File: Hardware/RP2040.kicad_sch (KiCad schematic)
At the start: 22 parts, among them U1 W25Q128JVS, U2 RP2040, Y1 ABM8-272-T3

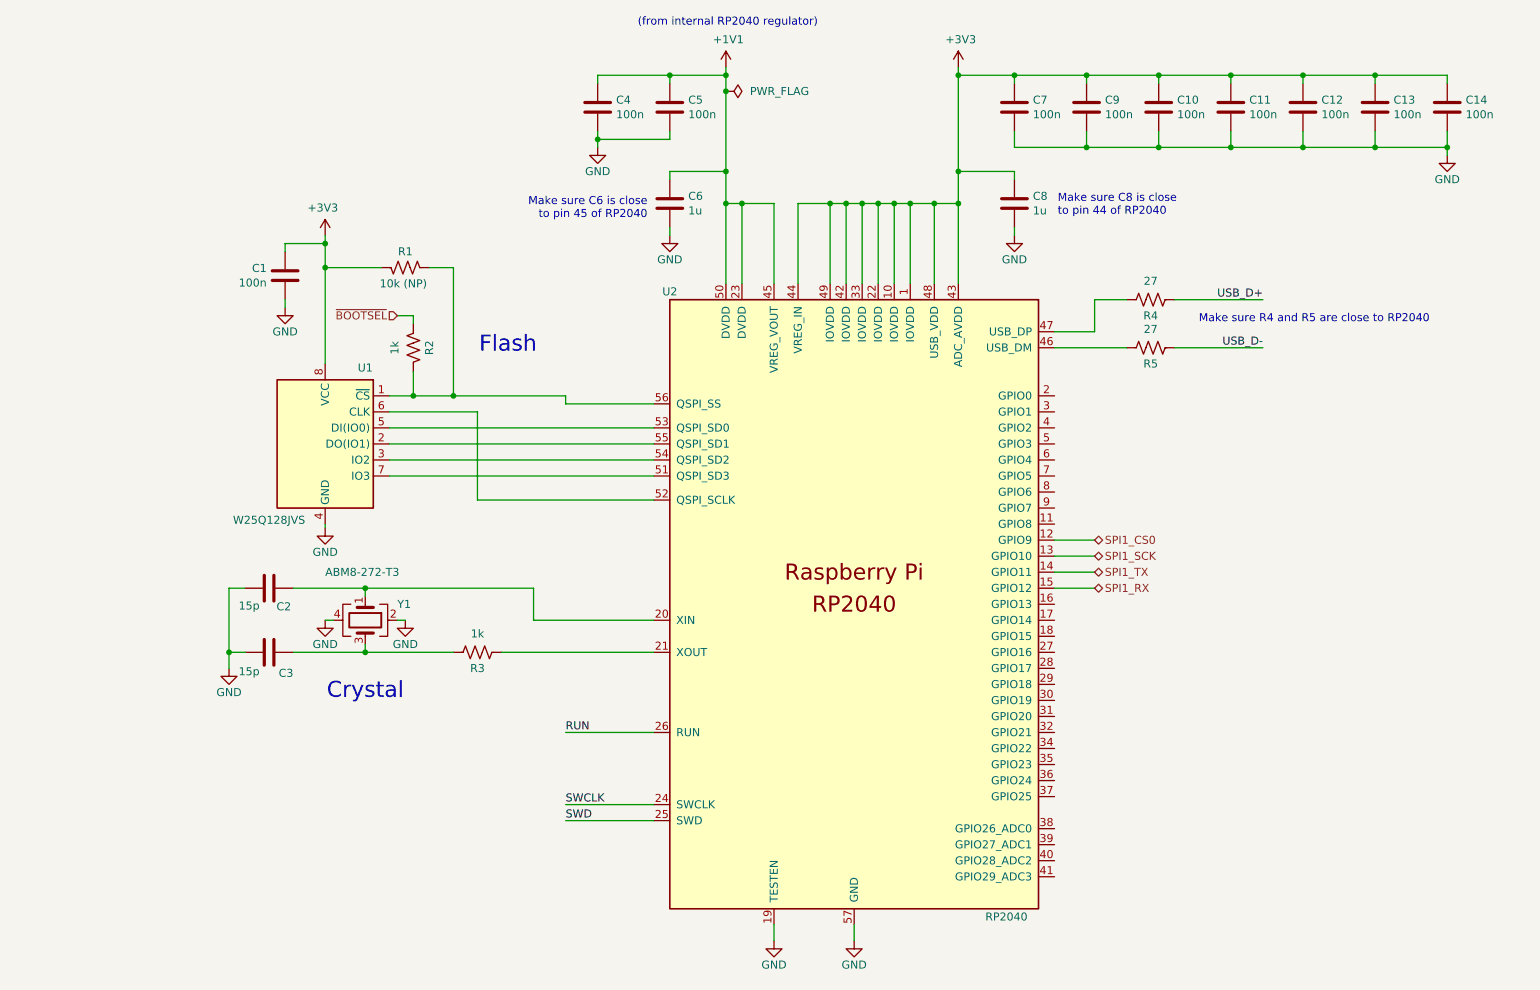
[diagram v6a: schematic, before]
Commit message: Add STM32 Reset Switch & RP2040 I2C pins
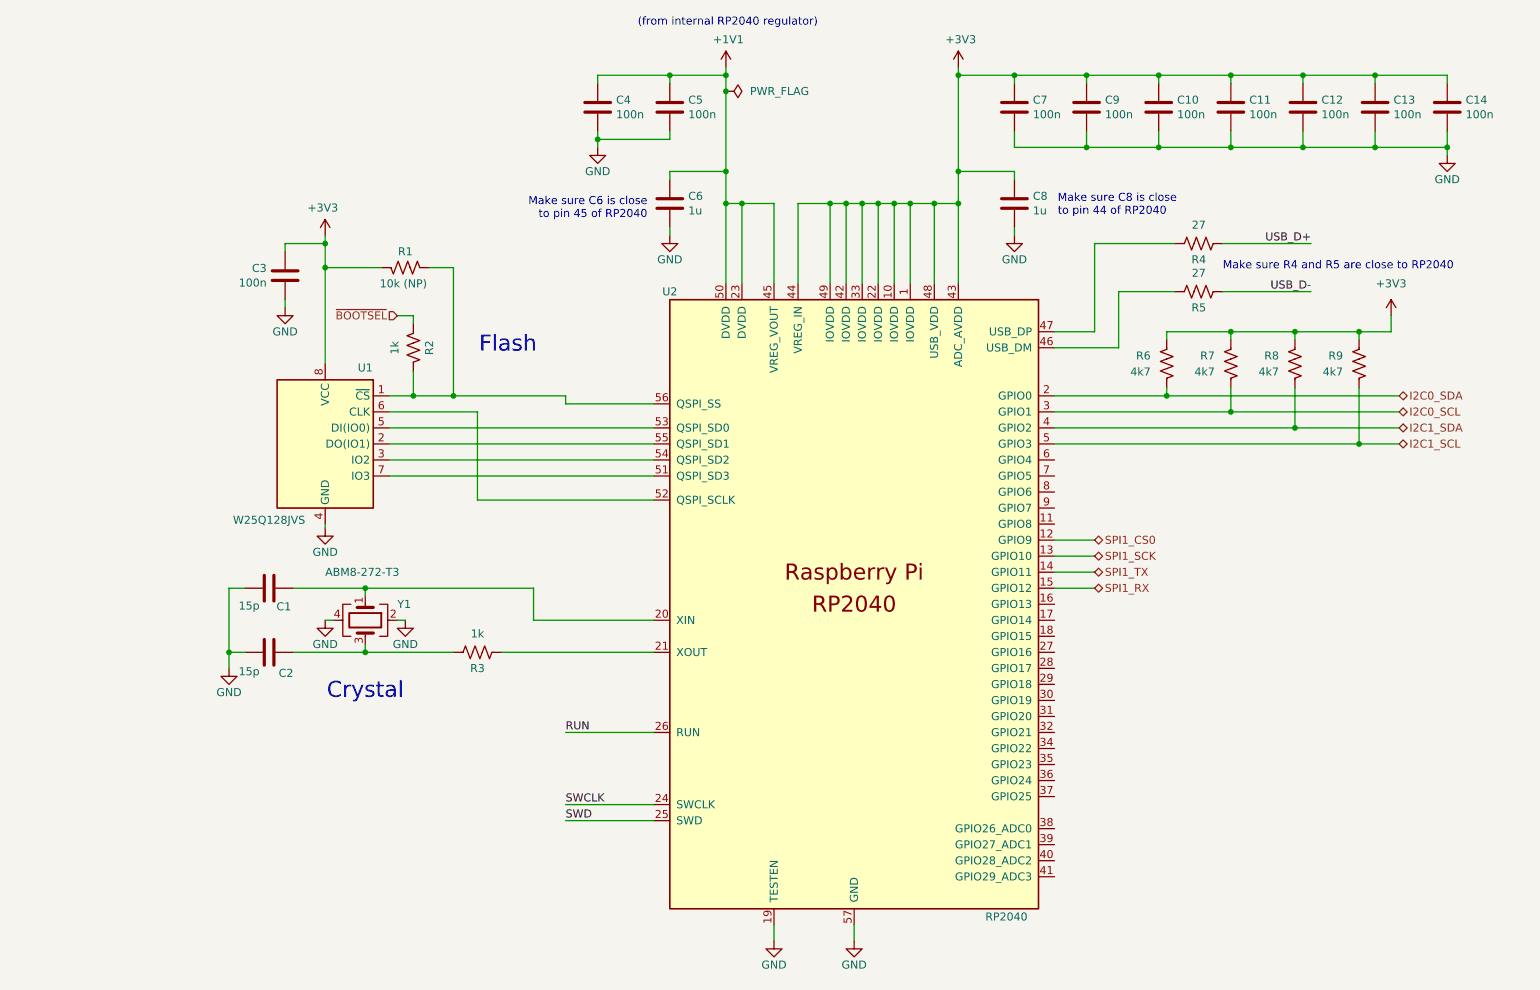
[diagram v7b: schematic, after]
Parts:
- added R6, R7, R8, R9: 4k7, symbol Device:R_US
- renumbered C2 to C1, C3 to C2, C1 to C3
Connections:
- net +3V3: now also R6.1, R7.1, R8.1, R9.1
- net I2C0_SDA: now reaches U2.2 (GPIO0)
- net I2C0_SDA: now also R6.2
- net I2C0_SCL: now reaches U2.3 (GPIO1)
- net I2C0_SCL: now also R7.2
- net I2C1_SDA: now reaches U2.4 (GPIO2)
- net I2C1_SDA: now also R8.2
- net I2C1_SCL: now reaches U2.5 (GPIO3)
- net I2C1_SCL: now also R9.2
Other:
- moved on the sheet: R4, R5

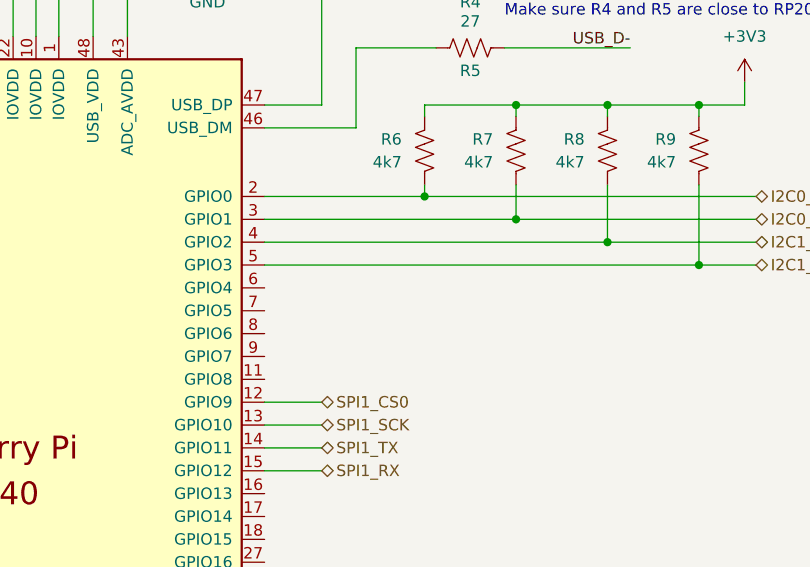
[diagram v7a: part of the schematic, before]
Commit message: Move ANT to RP2040
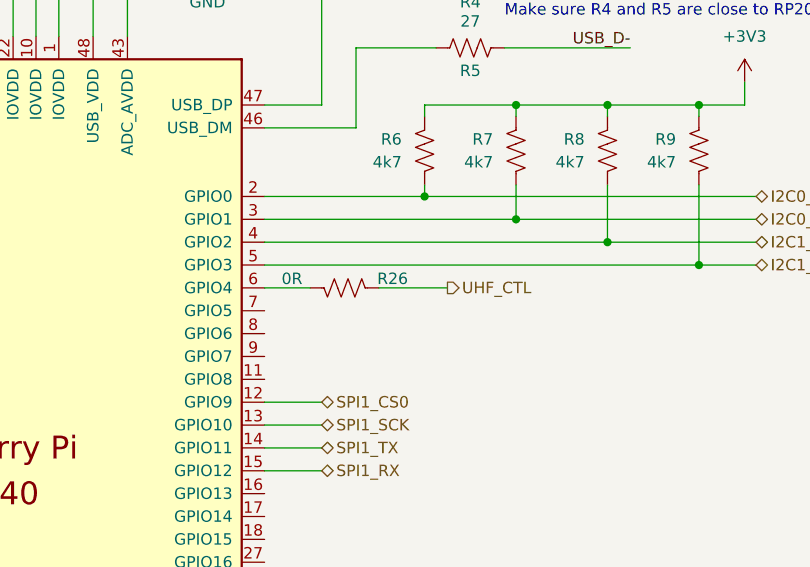
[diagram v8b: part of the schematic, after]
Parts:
- added R26: 0R, symbol Device:R_US
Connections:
- net at U2.6 (GPIO4): now also R26.2
- new net UHF_CTL: R26.1
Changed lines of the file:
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@@
 	(wire
 		(pts
+			(xy 243.84 123.19) (xy 238.76 123.19)
+		)
+		(stroke
+			(width 0)
+			(type default)
+		)
+	)
+	(wire
+		(pts
 			(xy 133.35 125.73) (xy 175.26 125.73)
 		)
@@
 	(wire
 		(pts
+			(xy 259.08 123.19) (xy 251.46 123.19)
+		)
+		(stroke
+			(width 0)
+			(type default)
+		)
+	)
+	(wire
+		(pts
 			(xy 255.27 63.5) (xy 255.27 62.23)
 		)
@@
 		)
 	)
+	(hierarchical_label "UHF_CTL"
+		(shape output)
+		(at 259.08 123.19 0)
+		(effects
+			(font
+				(size 1.27 1.27)
+			)
+			(justify left)
+		)
+	)
 	(hierarchical_label "I2C1_SCL"
 		(shape bidirectional)
@@
 					(unit 1)
 				)
+			)
+		)
+	)
+	(symbol
+		(lib_id "Device:R_US")
+		(at 247.65 123.19 270)
+		(mirror x)
+		(unit 1)
+		(exclude_from_sim no)
+		(in_bom yes)
+		(on_board yes)
+		(dnp no)
+		(property "Reference" "R26"
+			(at 252.984 122.174 90)
+			(effects
+				(font
+					(size 1.27 1.27)
+				)
+			)
+		)
+		(property "Value" "0R"
+			(at 241.808 122.174 90)
+			(effects
+				(font
+					(size 1.27 1.27)
+				)
+			)
+		)
+		(property "Footprint" ""
+			(at 247.396 122.174 90)
+			(effects
+				(font
+					(size 1.27 1.27)
+				)
+				(hide yes)
+			)
+		)
+		(property "Datasheet" "~"
+			(at 247.65 123.19 0)
+			(effects
+				(font
+					(size 1.27 1.27)
+				)
+				(hide yes)
+			)
+		)
+		(property "Description" "Resistor, US symbol"
+			(at 247.65 123.19 0)
+			(effects
+				(font
+					(size 1.27 1.27)
+				)
+				(hide yes)
+			)
+		)
+		(pin "2"
+		)
+		(pin "1"
+		)
+		(instances
+			(project "CTS-SAT-2-OBC-PCB"
+				(path "/58243925-df8d-4fc1-899e-fce866d1d25a/bec95c26-e44f-4f6a-97be-aee51e3bba5a"
+					(reference "R26")
+					(unit 1)
+				)
